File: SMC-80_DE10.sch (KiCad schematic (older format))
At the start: 6 parts, among them J1 Arduino1, J2 Arduino2, J3 DE10-Lite GPIO

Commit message: reorganized schematic, added missing pin label
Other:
- note added: "AA5"
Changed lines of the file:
@@
 encoding utf-8
 Sheet 1 2
-Title "DE10-Lite RAM/ROM/IDE Board"
-Date "2019-10-18"
+Title "SMC-80 Lite - Terasic DE10 Z80 Adapter Board"
+Date "2020-05-02"
 Rev "1.0"
 Comp "Hyiger Designs"
@@
 AB17
 NoConn ~ 4400 3900
+Text Notes 3650 3800 0    50   ~ 0
+AA5
 Wire Bus Line
 	6550 4100 6550 4500

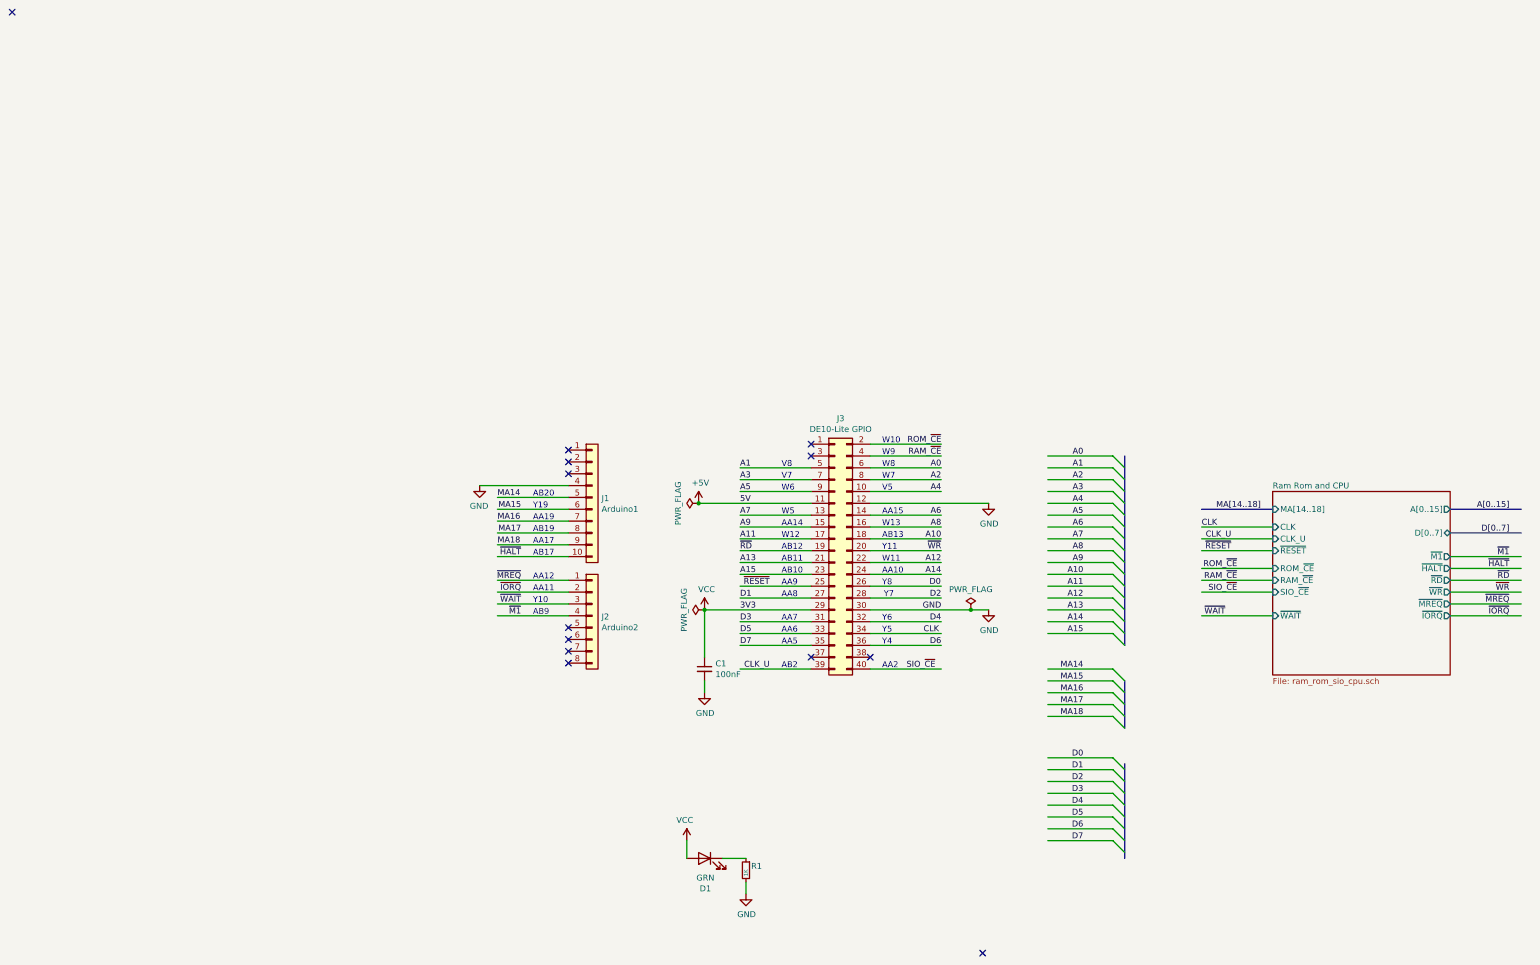
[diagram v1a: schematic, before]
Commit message: Broke out SIO C/D and B/A pins
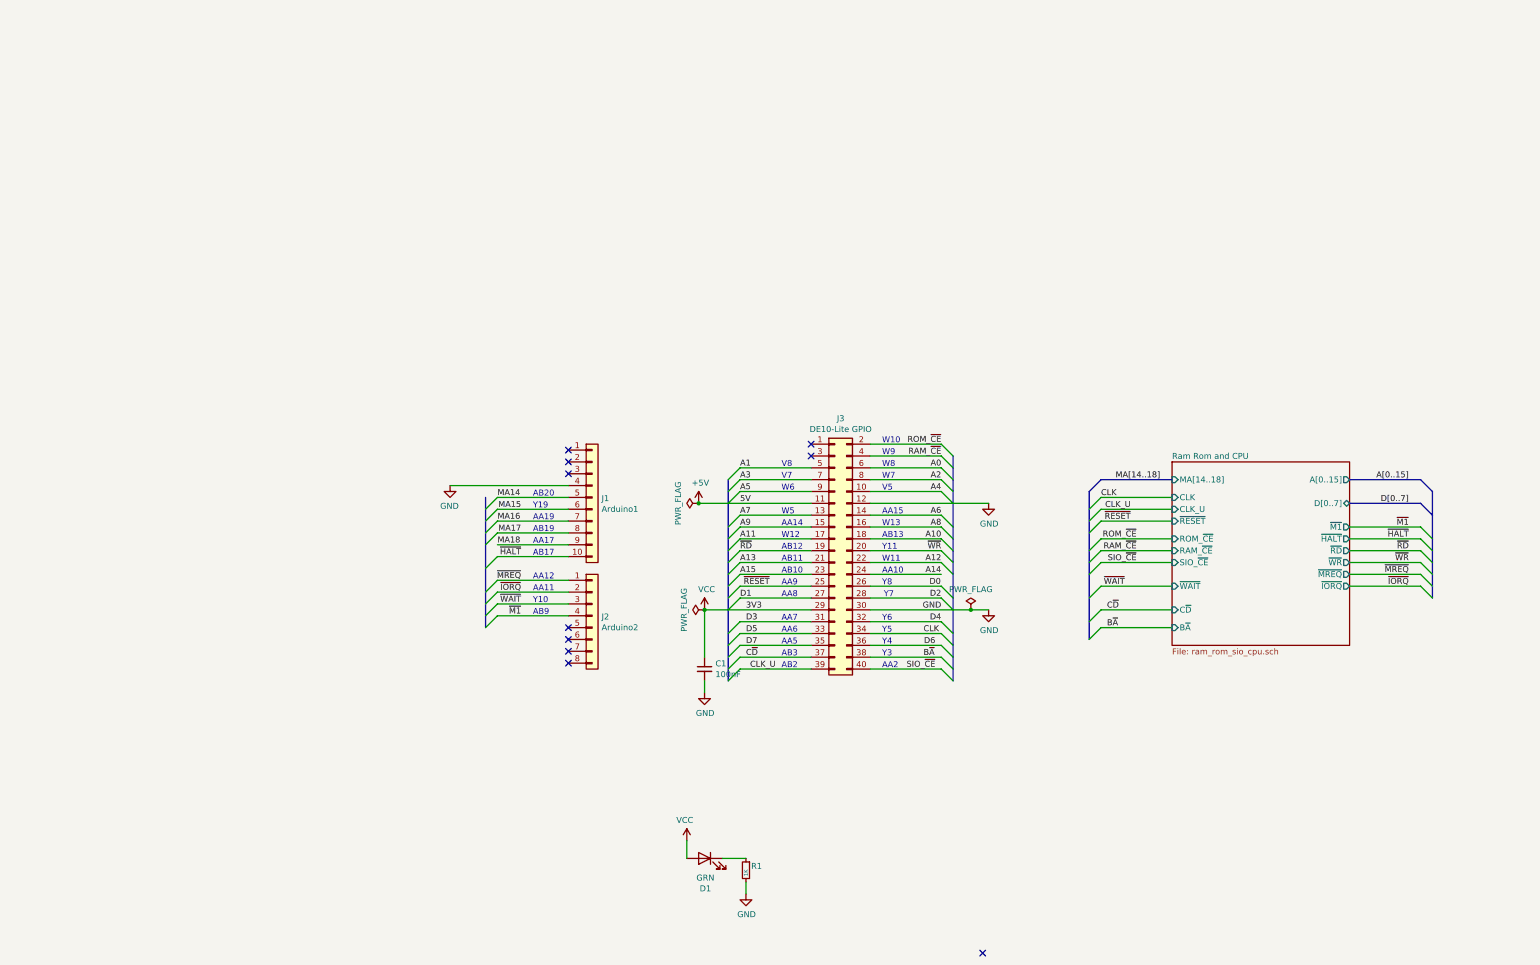
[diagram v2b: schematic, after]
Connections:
- net labels added: B~A, C~D
- wire segments 95 -> 70
- no-connect marks 13 -> 10
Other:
- note added: "AB3"
- note added: "Y3"
